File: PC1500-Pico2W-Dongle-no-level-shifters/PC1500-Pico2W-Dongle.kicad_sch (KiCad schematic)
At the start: 39 parts, among them J1 PC1500_60Pin_Connector, J2 microSD, J3 Spare GPIO (GP28), J5 GP2_Spare_IO, Q1 Si2333, Q2 MMBT2222A, U1 Pico2W, U2 AS6C62256-55SIN, U3 SLG46826G, U4 SLG46826G, U5 SC18IS602B, U7 AP1117-ADJ, U8 TCA9406DC

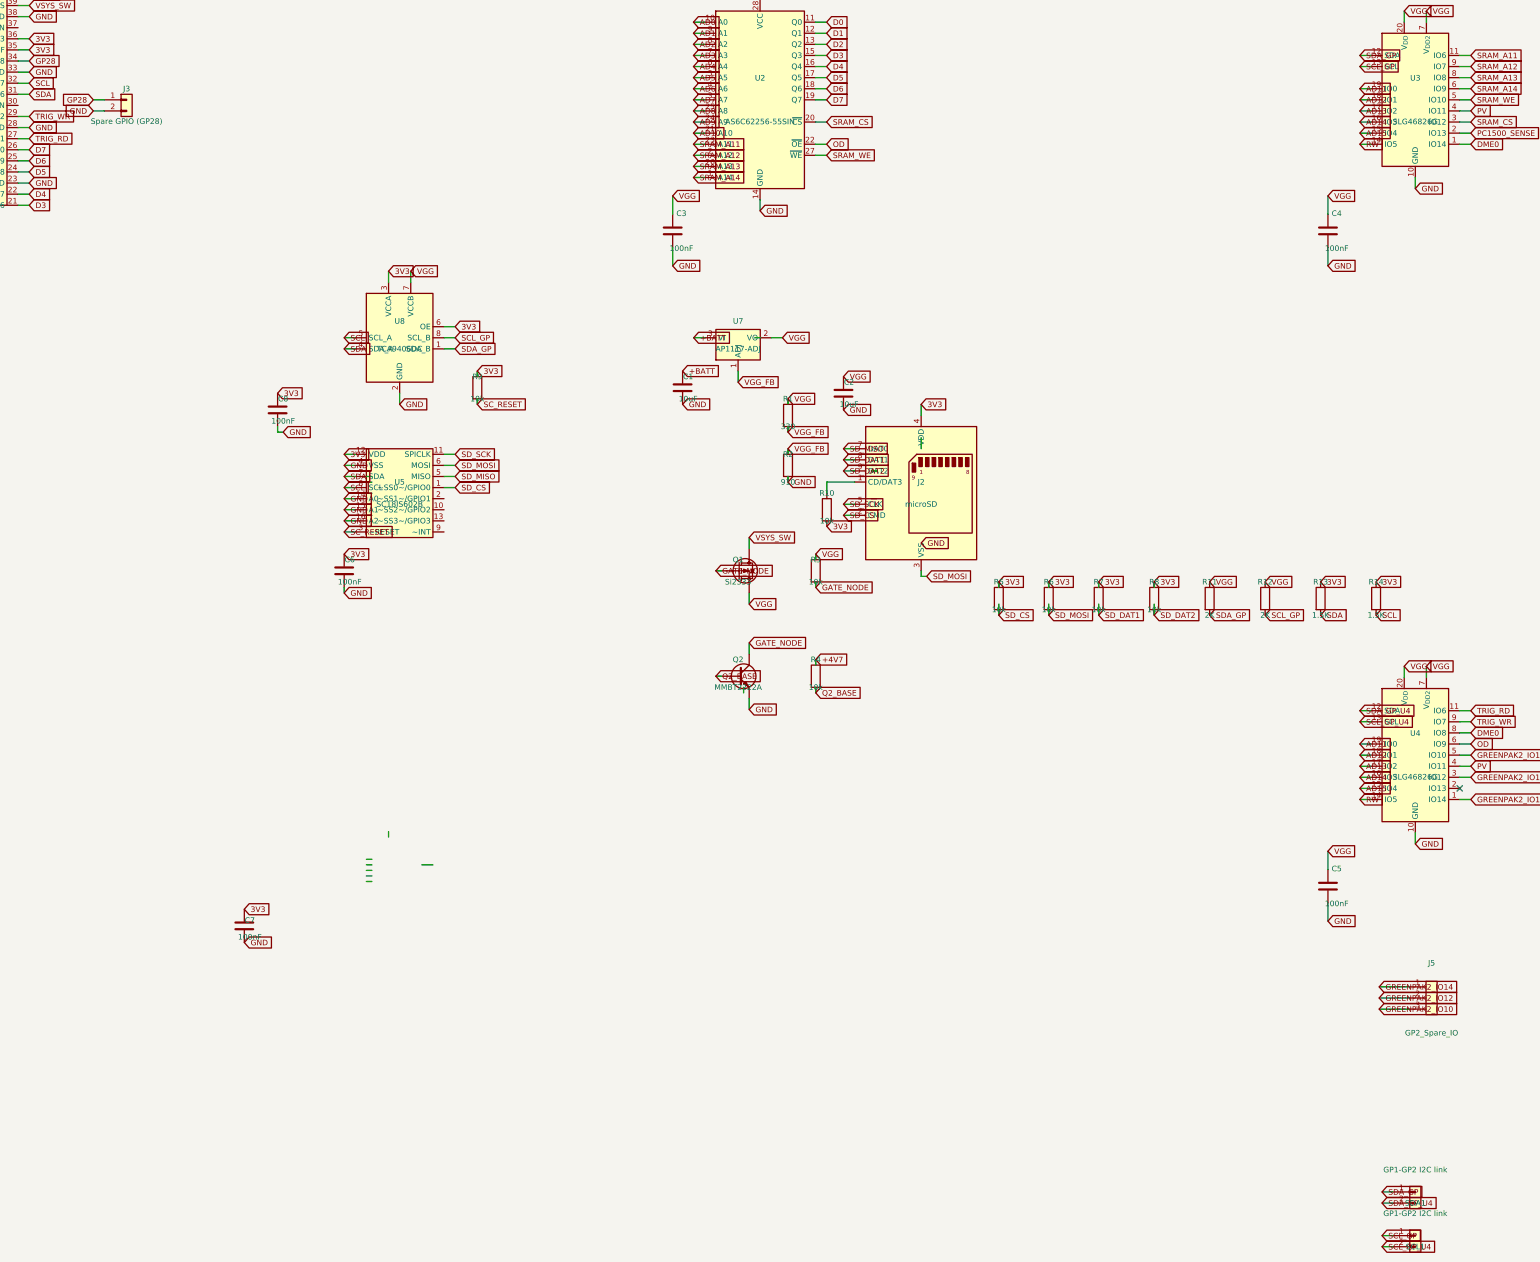
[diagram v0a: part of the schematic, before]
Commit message: Fix microSD pin 6 (GND) and pin 1 (unused, needs pull-up) on all 4 boards
Pin 6 and pin 3 were coincident in the generic SD_Card_Device symbol,
forcing GND onto the same net as CMD/MOSI. Relocated pin 6's local
coordinate and gave it its own wire+label on all four schematics
(RP2350B-BLE and Pico2W-Dongle, each with and without level shifters).

Pin 1 (symbol name CD/DAT3) is unused in this design but needs a 10K
pull-up to 3.3V rather than being left floating, matching the existing
SD_CS/SD_MOSI/SD_DAT1/SD_DAT2 pull-up pattern. Added the missing
wire+label+resistor to the three boards that lacked it
(Pico2W-Dongle-no-level-shifters already had it via R10).

Co-Authored-By: Claude Sonnet 5 <noreply@anthropic.com>
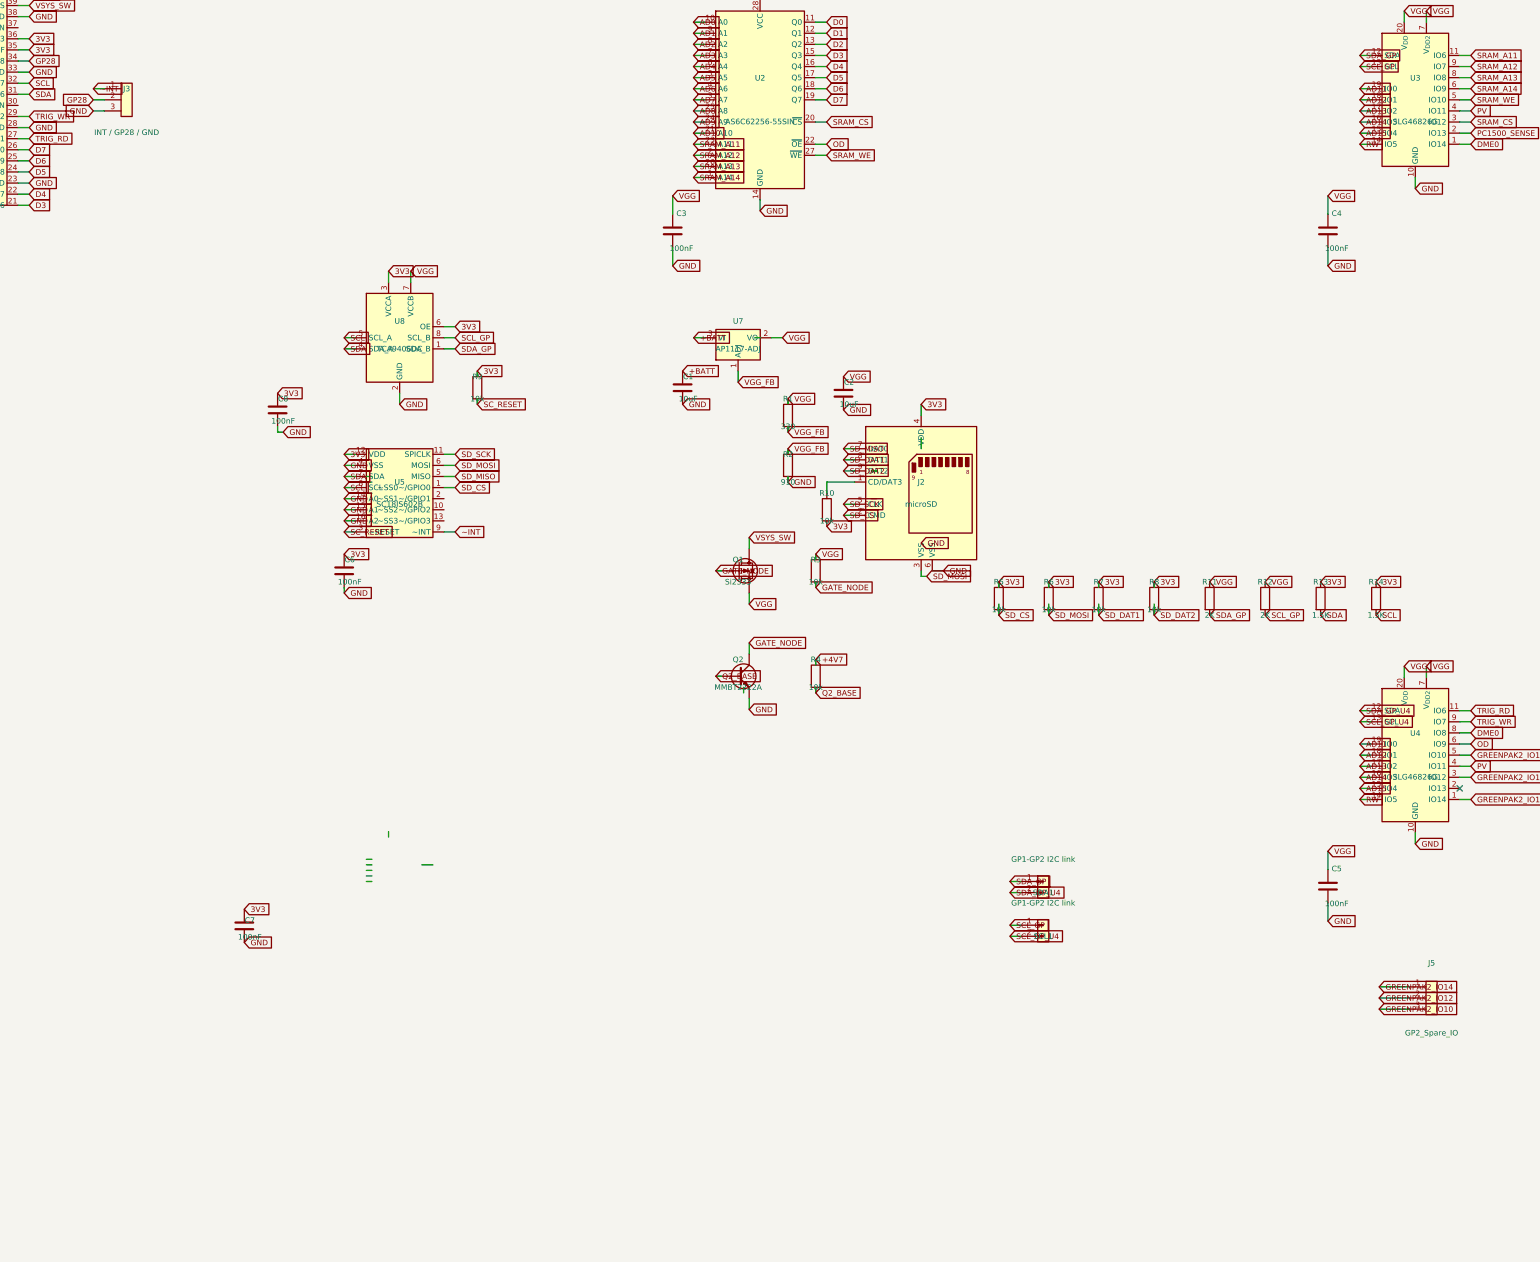
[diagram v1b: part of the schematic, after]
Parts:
- J3: value Spare GPIO (GP28) -> INT / GP28 / GND; footprint Connector_PinHeader_2.54mm:PinHeader_1x02_P2.54mm_Vertical -> Connector_PinHeader_2.54mm:PinHeader_1x03_P2.54mm_Vertical; symbol Connector_Generic:Conn_01x02 -> Connector_Generic:Conn_01x03
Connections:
- net GND: now also J2.6 (VSS), J3.3 (Pin_3); no longer J3.2 (Pin_2)
- net GP28: now also J3.2 (Pin_2); no longer J3.1 (Pin_1)
- net SD_MOSI: no longer J2.6 (VSS)
- net ~INT: now reaches U5.9 (~INT)
- net ~INT: now also J3.1 (Pin_1)
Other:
- moved on the sheet: J3, SCL1, SDA1

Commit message: Swap discontinued AP1117-ADJ for NCP1117-ADJ, clean up part names for BOM/CPL
AP1117-ADJ (U7, both Pico2W-Dongle variants) is discontinued; KiCad's own
library even flags it obsolete. Swapped to NCP1117-ADJ_SOT223, a
pin-compatible drop-in (same SOT-223 footprint, same graphics via the
library's "extends" relationship) - no rewiring needed. Had to embed the
new symbol into each schematic's symbol cache too, since just changing
the instance lib_id left it unresolvable and silently dropped from the
netlist/BOM.

Replaced dashes and underscores with spaces in all instance-level part
Values across both dongle boards, and in the no-level-shifters board's
exported BOM Footprint column and resistor values (added the missing
Ohm symbol) - all for cleaner JLCPCB/distributor part matching.

Co-Authored-By: Claude Sonnet 5 <noreply@anthropic.com>
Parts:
- J1: value PC1500_60Pin_Connector -> PC1500 60Pin Connector
- J5: value GP2_Spare_IO -> GP2 Spare IO
- SCL1, SDA1: value GP1-GP2 I2C link -> GP1 GP2 I2C link
- U2: value AS6C62256-55SIN -> AS6C62256 55SIN
- U7: value AP1117-ADJ -> NCP1117 ADJ; symbol Regulator_Linear:AP1117-ADJ -> Regulator_Linear:NCP1117-ADJ_SOT223
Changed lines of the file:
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@@
 	)
 	(symbol
-		(lib_id "Regulator_Linear:AP1117-ADJ")
+		(lib_id "Regulator_Linear:NCP1117-ADJ_SOT223")
 		(at 394.97 204.47 0)
 		(unit 1)
@@
 			)
 		)
-		(property "Value" "AP1117-ADJ"
+		(property "Value" "NCP1117 ADJ"
 			(at 394.97 207.01 0)
 			(show_name no)
@@
 			)
 		)
-		(property "Value" "PWR_FLAG"
+		(property "Value" "PWR FLAG"
 			(at 140 255 0)
 			(show_name no)
@@
 			)
 		)
-		(property "Value" "PWR_FLAG"
+		(property "Value" "PWR FLAG"
 			(at 100 255 0)
 			(show_name no)
@@
 			)
 		)
-		(property "Value" "AS6C62256-55SIN"
+		(property "Value" "AS6C62256 55SIN"
 			(at 400 155 0)
 			(show_name no)
@@
 			)
 		)
-		(property "Value" "GP2_Spare_IO"
+		(property "Value" "GP2 Spare IO"
 			(at 553.72 363.6 0)
 			(show_name no)
@@
 			)
 		)
-		(property "Value" "GP1-GP2 I2C link"
+		(property "Value" "GP1 GP2 I2C link"
 			(at 464.82 333.85 0)
 			(show_name no)
@@
 			)
 		)
-		(property "Value" "PC1500_60Pin_Connector"
+		(property "Value" "PC1500 60Pin Connector"
 			(at 50 155 0)
 			(show_name no)
@@
 			)
 		)
-		(property "Value" "GP1-GP2 I2C link"
+		(property "Value" "GP1 GP2 I2C link"
 			(at 464.82 323.85 0)
 			(show_name no)
@@
 			)
 		)
-		(property "Value" "PWR_FLAG"
+		(property "Value" "PWR FLAG"
 			(at 120 255 0)
 			(show_name no)

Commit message: Pico 2 W dongle (no level shifters): current schematic and PCB
The board owner's schematic and PCB as saved 2026-10-03/04.

Co-Authored-By: Claude Opus 5.5 <noreply@anthropic.com>
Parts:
- added R15: 4.7k, Resistor_SMD:R_0201_0603Metric, symbol Device:R
- R1, R2: footprint Resistor_SMD:R_0201_0603Metric -> Resistor_SMD:R_0603_1608Metric
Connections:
- net GND: now also Q2.2 (E), R15.2; no longer Q2.E
- net PU: now also J1.15 (PU); no longer J1.16 (PU)
- net PV: now also J1.16 (PV); no longer J1.15 (PV)
- net VGG: now also Q1.2 (S); no longer Q1.S
- net VSYS_SW: now also Q1.3 (D); no longer Q1.D
- net +4V7 renamed VCC
- removed net GATE_NODE: Q1.G, Q2.C, R3.2
- net Q2_BASE: no longer names the net of R4.2
- net Q2_BASE: now also Q2.1 (B), R15.1; no longer Q2.B
- new net: Q1.1 (G), Q2.3 (C), R3.2
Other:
- moved on the sheet: Q1, Q2, R3, R4
